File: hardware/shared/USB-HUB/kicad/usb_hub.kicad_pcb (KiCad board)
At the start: 2 copper layers, 54 x 26 mm, 28 parts, among them J1 SOFNG USB-05, SW1 BOOT_SERVICE, U1 ESP32-S3-MINI-1-N8, U2 RT9080-33GJ5

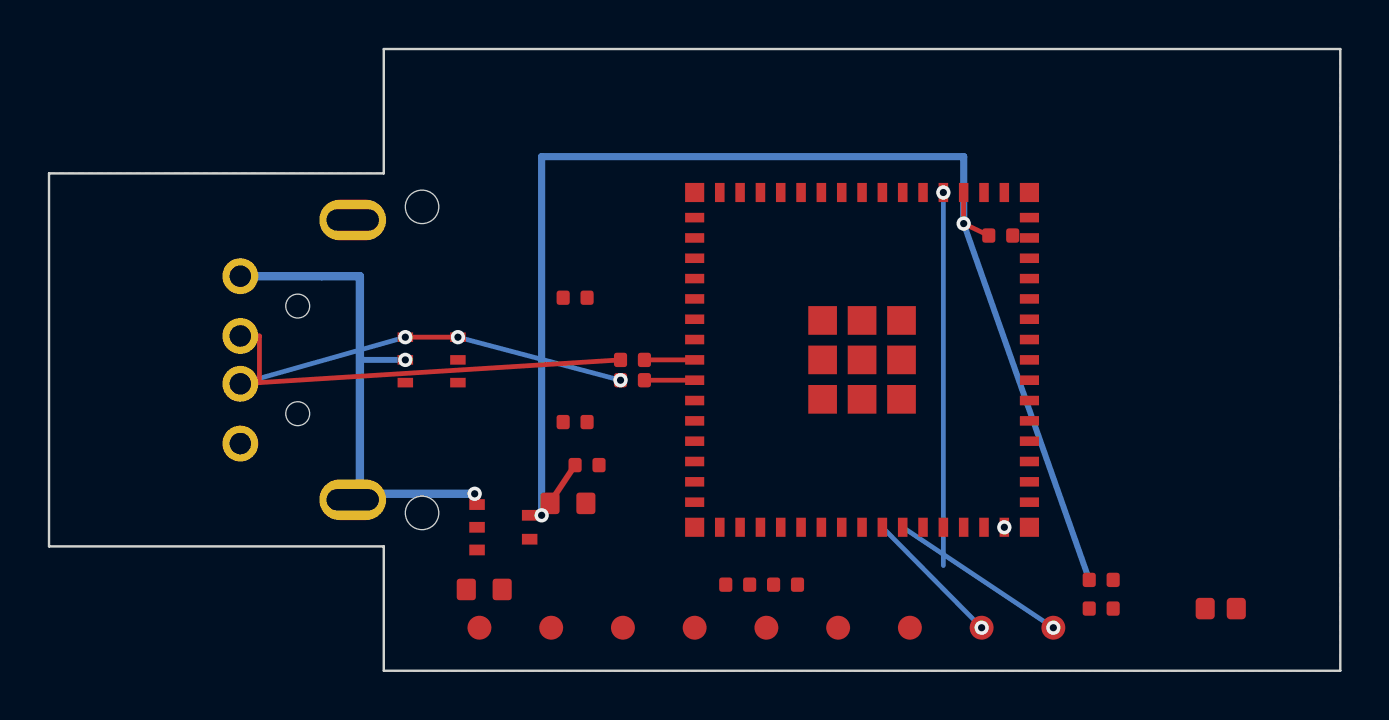
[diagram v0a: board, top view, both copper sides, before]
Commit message: feat(usb-hub): clean native USB first board pass
Sensing mechanism: none; native USB-A hub/control accessory capture for the shared USB-HUB packet.

Form factor and angle: direct-plug USB-A dongle first-board PCB; no ring angle applies.

Intended use case: offline native-USB repairable hub/control bring-up for accessibility pointing devices.

BOM estimate: kept inside the current USB-HUB approximately -6 first-board intent.
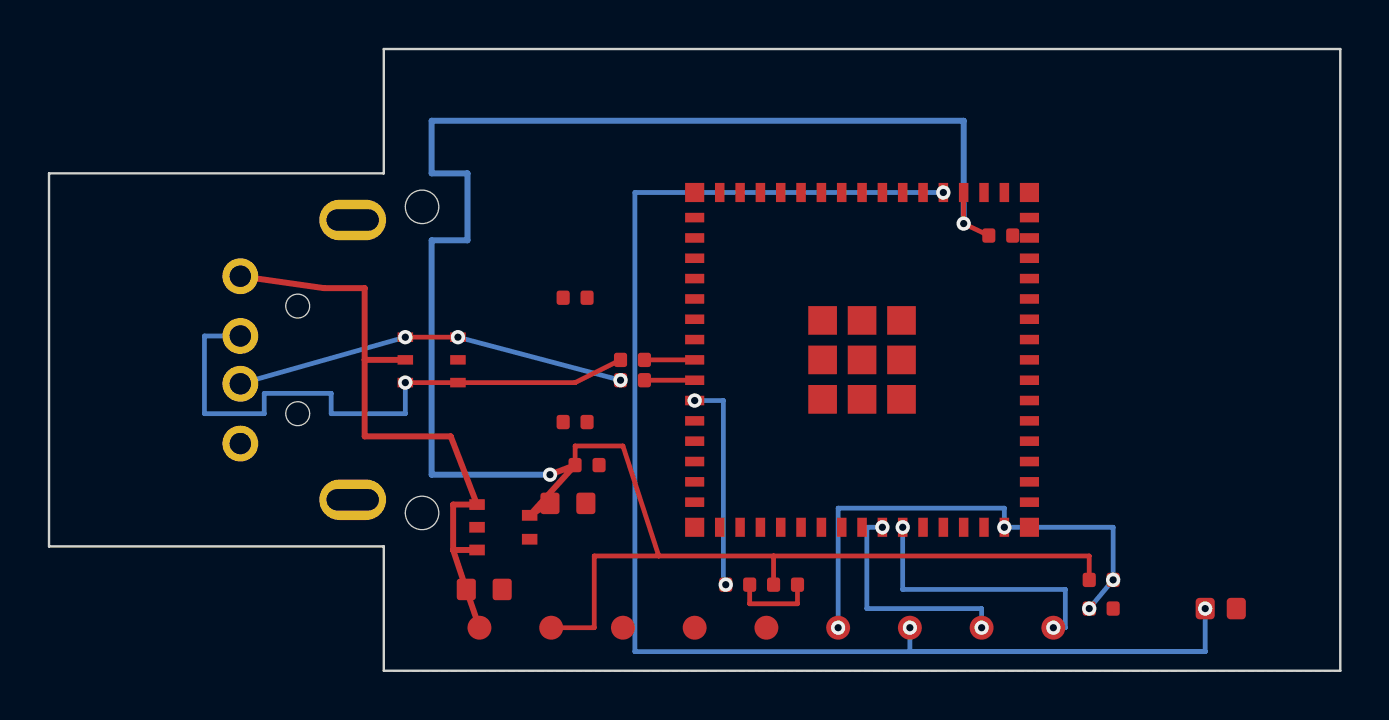
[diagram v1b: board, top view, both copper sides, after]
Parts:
- C5: value DNI USB_D- -> DNI USB_D- no-net
- C6: value DNI USB_D+ -> DNI USB_D+ no-net
- TP4: value D- -> D- trace access
- TP5: value D+ -> D+ trace access
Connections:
- C5 pad 1: USB_D- -> (no net)
- C5 pad 2: GND -> (no net)
- C6 pad 1: USB_D+ -> (no net)
- C6 pad 2: GND -> (no net)
- TP4 pad 1: USB_D- -> (no net)
- TP5 pad 1: USB_D+ -> (no net)
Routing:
- net BOOT_N: track 15.6 -> 71.1 mm, vias 1 -> 3
- net VREG_3V3: track 57.3 -> 92.0 mm
- net EN: track 0.00 -> 21.1 mm, vias 1 -> 4
- net LED_STATUS: track 0.00 -> 9.00 mm, vias 0 -> 2
- net USB_D-_CONN: track 17.9 -> 25.4 mm, vias 0 -> 1
- net VBUS_5V: track 21.3 -> 27.1 mm, vias 2 -> 0
- net UART_RX_DBG: track 7.57 -> 11.5 mm, vias 1 -> 2
- net UART_TX_DBG: track 5.90 -> 9.65 mm, vias 1 -> 2
- net LED_LIMIT: track 0.00 -> 3.60 mm

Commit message: fix(usb-hub): clean native-usb dongle drc parity
Direct-plug native USB hub dongle for accessibility pointing and OCR composition; no sensing mechanism change; BOM intent remains ~-6.
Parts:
- turned C2 to 180 degrees
- turned C3 to 180 degrees
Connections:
- net BOOT_N renamed /controls_and_indicators/BOOT_N
- net EN renamed /controls_and_indicators/EN
- net LED_LIMIT renamed /controls_and_indicators/LED_LIMIT
- net LED_STATUS renamed /controls_and_indicators/LED_STATUS
- net UART_RX_DBG renamed /controls_and_indicators/UART_RX_DBG
- net UART_TX_DBG renamed /controls_and_indicators/UART_TX_DBG
- net USB_D+ renamed /mcu_radio/USB_D+
- net USB_D+_CONN renamed /usb_and_power/USB_D+_CONN
- net USB_D- renamed /mcu_radio/USB_D-
- net USB_D-_CONN renamed /usb_and_power/USB_D-_CONN
- C1A pad 1: VREG_3V3 -> /controls_and_indicators/VREG_3V3
- C1A pad 2: GND -> /controls_and_indicators/GND
- C1B pad 1: VREG_3V3 -> /controls_and_indicators/VREG_3V3
- C1B pad 2: GND -> /controls_and_indicators/GND
- C2 pad 1: VBUS_5V -> /controls_and_indicators/GND
- C2 pad 2: GND -> /usb_and_power/VBUS_5V
- C3 pad 1: VREG_3V3 -> /controls_and_indicators/GND
- C3 pad 2: GND -> /controls_and_indicators/VREG_3V3
- C4 pad 2: GND -> /controls_and_indicators/GND
- D1 pad 2: GND -> /controls_and_indicators/GND
- D1 pad 5: VBUS_5V -> /usb_and_power/VBUS_5V
- J1 pad 1: VBUS_5V -> /usb_and_power/VBUS_5V
- J1 pad 4: GND -> /controls_and_indicators/GND
- J1 pad SH1: GND -> /controls_and_indicators/GND
- J1 pad SH2: GND -> /controls_and_indicators/GND
- R2 pad 1: VREG_3V3 -> /controls_and_indicators/VREG_3V3
- R3 pad 1: VREG_3V3 -> /controls_and_indicators/VREG_3V3
- SW1 pad 2: GND -> /controls_and_indicators/GND
- TP1 pad 1: VBUS_5V -> /usb_and_power/VBUS_5V
- TP2 pad 1: VREG_3V3 -> /controls_and_indicators/VREG_3V3
- TP3 pad 1: GND -> /controls_and_indicators/GND
- U1 pad 1: GND -> /controls_and_indicators/GND
- U1 pad 2: GND -> /controls_and_indicators/GND
- U1 pad 3: VREG_3V3 -> /controls_and_indicators/VREG_3V3
- U1 pad 42: GND -> /controls_and_indicators/GND
- U1 pad 43: GND -> /controls_and_indicators/GND
- U1 pad 46: GND -> /controls_and_indicators/GND
- U1 pad 47: GND -> /controls_and_indicators/GND
- U1 pad 48: GND -> /controls_and_indicators/GND
- U1 pad 49: GND -> /controls_and_indicators/GND
- U1 pad 50: GND -> /controls_and_indicators/GND
- U1 pad 51: GND -> /controls_and_indicators/GND
- U1 pad 52: GND -> /controls_and_indicators/GND
- U1 pad 53: GND -> /controls_and_indicators/GND
- U1 pad 54: GND -> /controls_and_indicators/GND
- U1 pad 55: GND -> /controls_and_indicators/GND
- U1 pad 56: GND -> /controls_and_indicators/GND
- U1 pad 57: GND -> /controls_and_indicators/GND
- U1 pad 58: GND -> /controls_and_indicators/GND
- U1 pad 59: GND -> /controls_and_indicators/GND
- U1 pad 60: GND -> /controls_and_indicators/GND
- U1 pad 61: GND -> /controls_and_indicators/GND
- U1 pad 62: GND -> /controls_and_indicators/GND
- U1 pad 63: GND -> /controls_and_indicators/GND
- U1 pad 64: GND -> /controls_and_indicators/GND
- U1 pad 65: GND -> /controls_and_indicators/GND
- U2 pad 1: VBUS_5V -> /usb_and_power/VBUS_5V
- U2 pad 2: GND -> /controls_and_indicators/GND
- U2 pad 3: VBUS_5V -> /usb_and_power/VBUS_5V
- U2 pad 5: VREG_3V3 -> /controls_and_indicators/VREG_3V3
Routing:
- net /controls_and_indicators/VREG_3V3: track 0.00 -> 92.0 mm, vias 0 -> 2
- net VREG_3V3: track 92.0 -> 0.00 mm, vias 2 -> 0
- net VBUS_5V: track 27.1 -> 0.00 mm
- net /usb_and_power/VBUS_5V: track 0.00 -> 27.1 mm
- added copper zone on B.Cu, net /controls_and_indicators/GND
- added copper zone on F.Cu, net /controls_and_indicators/GND
- removed copper zone on B.Cu, net GND
- removed copper zone on F.Cu, net GND

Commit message: fix(usb-hub): pin local first-board footprints
Design disclosure: sensing mechanism none; form factor stepped USB-A direct-plug USB-HUB dongle; intended use offline BLE HID composition and service access for accessibility; BOM estimate ~$5-6 packet target.

Move first-board commodity/support footprints into the source-controlled PowerFinger_USB library and update the packet verification story to all-severity PCB DRC clean.
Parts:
- C1A, C1B, C4, C5, C6: footprint Capacitor_SMD:C_0402_1005Metric -> PowerFinger_USB:C_0402_1005Metric_FirstBoard
- C2, C3: footprint Capacitor_SMD:C_0603_1608Metric -> PowerFinger_USB:C_0603_1608Metric_FirstBoard
- D1: footprint Package_TO_SOT_SMD:SOT-23-6 -> PowerFinger_USB:SOT-23-6_FirstBoard
- LED1: footprint LED_SMD:LED_0402_1005Metric -> PowerFinger_USB:LED_0402_1005Metric_FirstBoard
- MH1, MH2: footprint MountingHole:MountingHole_1.4mm -> PowerFinger_USB:MountingHole_1.4mm_Clamp
- R1A, R1B, R2, R3: footprint Resistor_SMD:R_0402_1005Metric -> PowerFinger_USB:R_0402_1005Metric_FirstBoard
- TP1, TP2, TP3, TP4, TP5, TP6, TP7, TP8, TP9: footprint TestPoint:TestPoint_Pad_D1.0mm -> PowerFinger_USB:TestPoint_Pad_D1.0mm_FirstBoard
- U2: footprint Package_TO_SOT_SMD:SOT-23-5 -> PowerFinger_USB:SOT-23-5_FirstBoard
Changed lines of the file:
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@@
 		)
 	)
-	(footprint "Package_TO_SOT_SMD:SOT-23-5"
+	(footprint "PowerFinger_USB:SOT-23-5_FirstBoard"
 		(layer "F.Cu")
 		(at 19 20)
@@
 		(embedded_fonts no)
 	)
-	(footprint "Capacitor_SMD:C_0402_1005Metric"
+	(footprint "PowerFinger_USB:C_0402_1005Metric_FirstBoard"
 		(layer "F.Cu")
 		(at 22.5 17.4)
@@
 		(embedded_fonts no)
 	)
-	(footprint "TestPoint:TestPoint_Pad_D1.0mm"
+	(footprint "PowerFinger_USB:TestPoint_Pad_D1.0mm_FirstBoard"
 		(layer "F.Cu")
 		(at 33 24.2)
@@
 		(embedded_fonts no)
 	)
-	(footprint "TestPoint:TestPoint_Pad_D1.0mm"
+	(footprint "PowerFinger_USB:TestPoint_Pad_D1.0mm_FirstBoard"
 		(layer "F.Cu")
 		(at 24 24.2)
@@
 		(embedded_fonts no)
 	)
-	(footprint "Resistor_SMD:R_0402_1005Metric"
+	(footprint "PowerFinger_USB:R_0402_1005Metric_FirstBoard"
 		(layer "F.Cu")
 		(at 24.4 13.85)
@@
 		(embedded_fonts no)
 	)
-	(footprint "MountingHole:MountingHole_1.4mm"
+	(footprint "PowerFinger_USB:MountingHole_1.4mm_Clamp"
 		(layer "F.Cu")
 		(at 15.6 19.4)
@@
 		(embedded_fonts no)
 	)
-	(footprint "Capacitor_SMD:C_0603_1608Metric"
+	(footprint "PowerFinger_USB:C_0603_1608Metric_FirstBoard"
 		(layer "F.Cu")
 		(at 18.2 22.6 180)
@@
 		(embedded_fonts no)
 	)
-	(footprint "Capacitor_SMD:C_0402_1005Metric"
+	(footprint "PowerFinger_USB:C_0402_1005Metric_FirstBoard"
 		(layer "F.Cu")
 		(at 22 15.6)
@@
 		(embedded_fonts no)
 	)
-	(footprint "LED_SMD:LED_0402_1005Metric"
+	(footprint "PowerFinger_USB:LED_0402_1005Metric_FirstBoard"
 		(layer "F.Cu")
 		(at 28.8 22.4)
@@
 		(embedded_fonts no)
 	)
-	(footprint "Capacitor_SMD:C_0402_1005Metric"
+	(footprint "PowerFinger_USB:C_0402_1005Metric_FirstBoard"
 		(layer "F.Cu")
 		(at 22 10.4)
@@
 		(embedded_fonts no)
 	)
-	(footprint "TestPoint:TestPoint_Pad_D1.0mm"
+	(footprint "PowerFinger_USB:TestPoint_Pad_D1.0mm_FirstBoard"
 		(layer "F.Cu")
 		(at 18 24.2)
@@
 		(embedded_fonts no)
 	)
-	(footprint "Package_TO_SOT_SMD:SOT-23-6"
+	(footprint "PowerFinger_USB:SOT-23-6_FirstBoard"
 		(layer "F.Cu")
 		(at 16 13 180)
@@
 		(embedded_fonts no)
 	)
-	(footprint "Capacitor_SMD:C_0402_1005Metric"
+	(footprint "PowerFinger_USB:C_0402_1005Metric_FirstBoard"
 		(layer "F.Cu")
 		(at 44 23.4)
@@
 		(embedded_fonts no)
 	)
-	(footprint "Resistor_SMD:R_0402_1005Metric"
+	(footprint "PowerFinger_USB:R_0402_1005Metric_FirstBoard"
 		(layer "F.Cu")
 		(at 30.8 22.4)
@@
 		(embedded_fonts no)
 	)
-	(footprint "TestPoint:TestPoint_Pad_D1.0mm"
+	(footprint "PowerFinger_USB:TestPoint_Pad_D1.0mm_FirstBoard"
 		(layer "F.Cu")
 		(at 36 24.2)
@@
 		(embedded_fonts no)
 	)
-	(footprint "TestPoint:TestPoint_Pad_D1.0mm"
+	(footprint "PowerFinger_USB:TestPoint_Pad_D1.0mm_FirstBoard"
 		(layer "F.Cu")
 		(at 39 24.2)
@@
 		(embedded_fonts no)
 	)
-	(footprint "Capacitor_SMD:C_0402_1005Metric"
+	(footprint "PowerFinger_USB:C_0402_1005Metric_FirstBoard"
 		(layer "F.Cu")
 		(at 39.8 7.8)
@@
 		(embedded_fonts no)
 	)
-	(footprint "Resistor_SMD:R_0402_1005Metric"
+	(footprint "PowerFinger_USB:R_0402_1005Metric_FirstBoard"
 		(layer "F.Cu")
 		(at 24.4 13)
@@
 		(embedded_fonts no)
 	)
-	(footprint "TestPoint:TestPoint_Pad_D1.0mm"
+	(footprint "PowerFinger_USB:TestPoint_Pad_D1.0mm_FirstBoard"
 		(layer "F.Cu")
 		(at 42 24.2)
@@
 		(embedded_fonts no)
 	)
-	(footprint "Capacitor_SMD:C_0603_1608Metric"
+	(footprint "PowerFinger_USB:C_0603_1608Metric_FirstBoard"
 		(layer "F.Cu")
 		(at 21.7 19 180)
@@
 		(embedded_fonts no)
 	)
-	(footprint "TestPoint:TestPoint_Pad_D1.0mm"
+	(footprint "PowerFinger_USB:TestPoint_Pad_D1.0mm_FirstBoard"
 		(layer "F.Cu")
 		(at 30 24.2)
@@
 		(embedded_fonts no)
 	)
-	(footprint "TestPoint:TestPoint_Pad_D1.0mm"
+	(footprint "PowerFinger_USB:TestPoint_Pad_D1.0mm_FirstBoard"
 		(layer "F.Cu")
 		(at 21 24.2)
@@
 		(embedded_fonts no)
 	)
-	(footprint "TestPoint:TestPoint_Pad_D1.0mm"
+	(footprint "PowerFinger_USB:TestPoint_Pad_D1.0mm_FirstBoard"
 		(layer "F.Cu")
 		(at 27 24.2)
@@
 		(embedded_fonts no)
 	)
-	(footprint "Resistor_SMD:R_0402_1005Metric"
+	(footprint "PowerFinger_USB:R_0402_1005Metric_FirstBoard"
 		(layer "F.Cu")
 		(at 44 22.2)
@@
 		(embedded_fonts no)
 	)
-	(footprint "MountingHole:MountingHole_1.4mm"
+	(footprint "PowerFinger_USB:MountingHole_1.4mm_Clamp"
 		(layer "F.Cu")
 		(at 15.6 6.6)
